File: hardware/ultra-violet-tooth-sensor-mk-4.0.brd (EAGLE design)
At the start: 51 x 23 mm, 13 parts, among them IC1 SI1145QFN10, U1 ADAFRUIT_BLUEFRUIT_LE_MICRO, U2 ADAFRUIT-SI1145-BREAKOUTHOLEY

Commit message: simblee based uvdosimeter
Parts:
- removed BATT: M02PTH-CENTERED-R+, A_butts:1X02-CENTER-R+
- removed IC1: SI1145QFN10, A_butts:SI1145
- removed POWER: SWITCH-SPDTPTH-RA-2.54MM, A_butts:SPDT-RA-2.54MM
- added BAT: M02JST-PTH-RA-R+, a_parts:JST-2-PH-RA-PTH-R+
- added C3, C8: 10u, a_parts:C0603
- added C4: 10nF, a_parts:C0603
- added C5: 4u7, a_parts:C0603
- added C6: 100n, a_parts:C0603
- added C7: 0.1uF, a_parts:C0603
- added CHRG, DONE: LED0603, a_parts:LED-0603
- added D1: (no value), a_parts:SOD123-SCHOTTKY
- added DISP1: ER-OLED0.49-1FOLDED-SAME, a_parts:ER-OLED0.49-1-FOLDED-SAME
- added Q1: (no value), a_parts:SOT23
- added R1: 10K, a_parts:R0603
- added R4: 1K, a_parts:R0603
- added R5: 100K, a_parts:R0603
- added RESET: SPST-NO-TACTSMD-TINIER, a_parts:TACTILE_SWITCH_SMD_TINY
- added U3: MCP73831T-2ACI/OT, a_parts:SOT95P280X145-5N
- added U4: V_REG_SOT-23-5AS13985, a_parts:SOT23-5
- added U5: VEML6075, a_parts:OPLGA4
- added U6: TCS3400DFN6, a_parts:TCS3400_DFN6
- added USB: (no value), a_parts:FCI-10103594-USB-MICRO-B-LESS
- C1: device A_butts:C0805 -> a_parts:C0603
- C2: value 0.1uF -> 10u; device A_butts:C0805 -> a_parts:C0603
- FRAME1: value (none) -> FRAME-LETTERNO_PACKAGE
- R2: value 100k -> 330R; device A_butts:R0805 -> a_parts:R0603
- R3: value 100k -> 2K; device A_butts:R0805 -> a_parts:R0603
- U1: value ADAFRUIT_BLUEFRUIT_LE_MICRO -> SIMBLEE-RFD77101; device A_butts:ADAFRUIT_BLUEFRUIT_LE_MICRO -> a_parts:RFD77101
- U2: value ADAFRUIT-SI1145-BREAKOUTHOLEY -> FTS31XS-U; device A_butts:ADAFRUIT-SI1145-BREAKOUT -> a_parts:SSOP20_L
- moved R2 135.7 mm to (-38.4, -67.8), turned to 0 degrees
- moved R3 125.3 mm to (-38.4, -58.9), turned to 0 degrees
- moved U2 46.9 mm to (-4.50, -14.7), turned to 0 degrees
- moved U1 31.5 mm to (-5.30, 4.80)
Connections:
- removed net SCL: IC1.SCL, R3.1, U1.3/SCL, U2.SCL
- removed net SDA: IC1.SDA, R2.1, U1.2/SDA, U2.SDA
- new net DTR: C4.1
- new net N$2: CHRG.C, DONE.A, R2.1
- new net N$3: U2.11, USB.3
- new net N$4: U2.12, USB.2
- new net N$5: R3.2, U3.5
- new net N$6: R2.2, U3.1
- new net N$9: C6.1, U4.3
- new net RESET: C4.2, R1.1, RESET.P$2, U1.8
- new net VBAT: BAT.2, C5.1, Q1.3, U3.3
- new net VIN: C2.1, D1.C, Q1.2, U4.1, U4.4
- new net VUSB: CHRG.A, D1.A, Q1.1, R5.2, U2.15, U3.4, USB.1
- net 3.3V: now also C3.1, C7.1, R1.2, U1.7, U2.14, U2.3, U4.5; no longer C2.1, IC1.VCC@1, IC1.VCC@2, IC1.VCC@3, R2.2, R3.2, U1.3V3, U2.3V3_OUT
- net GND: now also BAT.1, C3.2, C5.2, C6.2, C7.2, DONE.C, R3.1, R5.1, RESET.P$1, U1.1, U1.19, U1.2, U1.30, U1.4, U1.42, U1.43, U1.44, U1.45, U1.6, U2.16, U2.6, U3.2, U4.2, USB.5; no longer IC1.GND, U1.GND@1, U1.GND@2, U1.GND@3, U2.GND

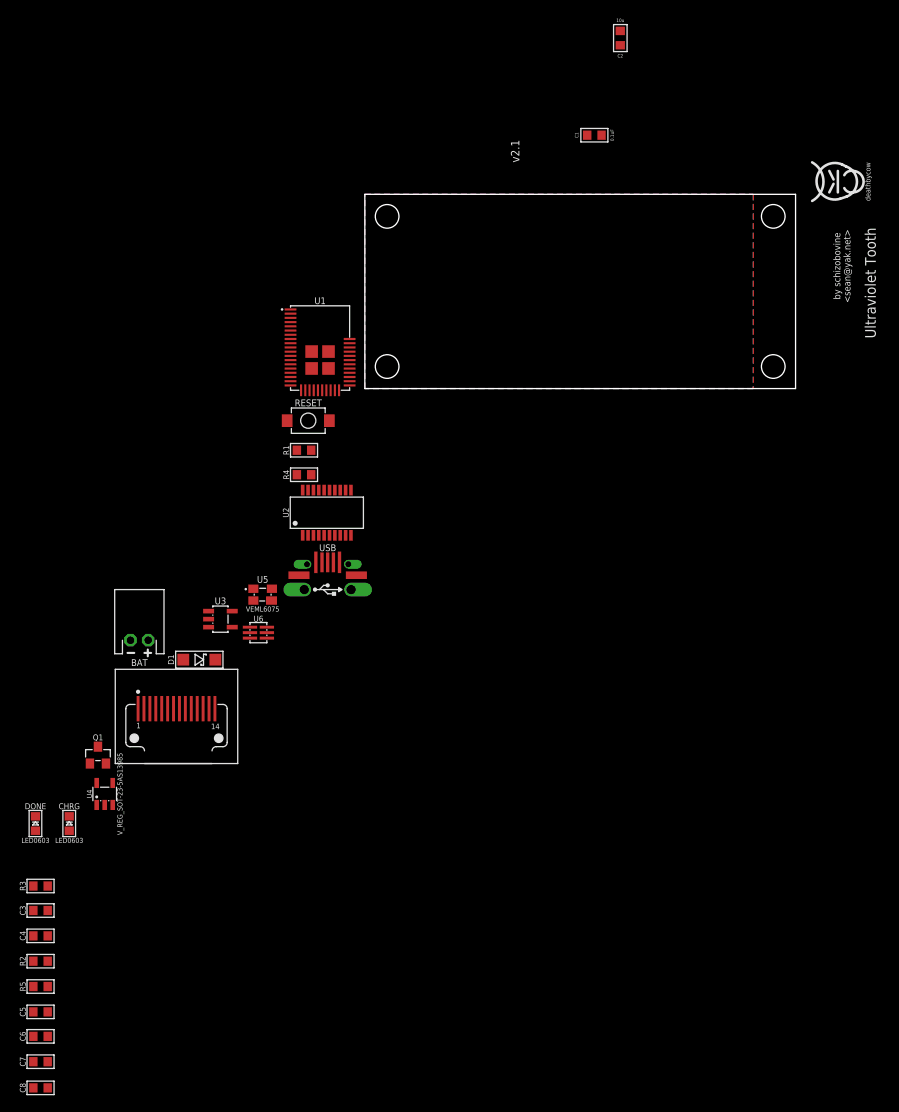
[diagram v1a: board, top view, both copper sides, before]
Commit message: more fiddling, need smaller usb to uart chip
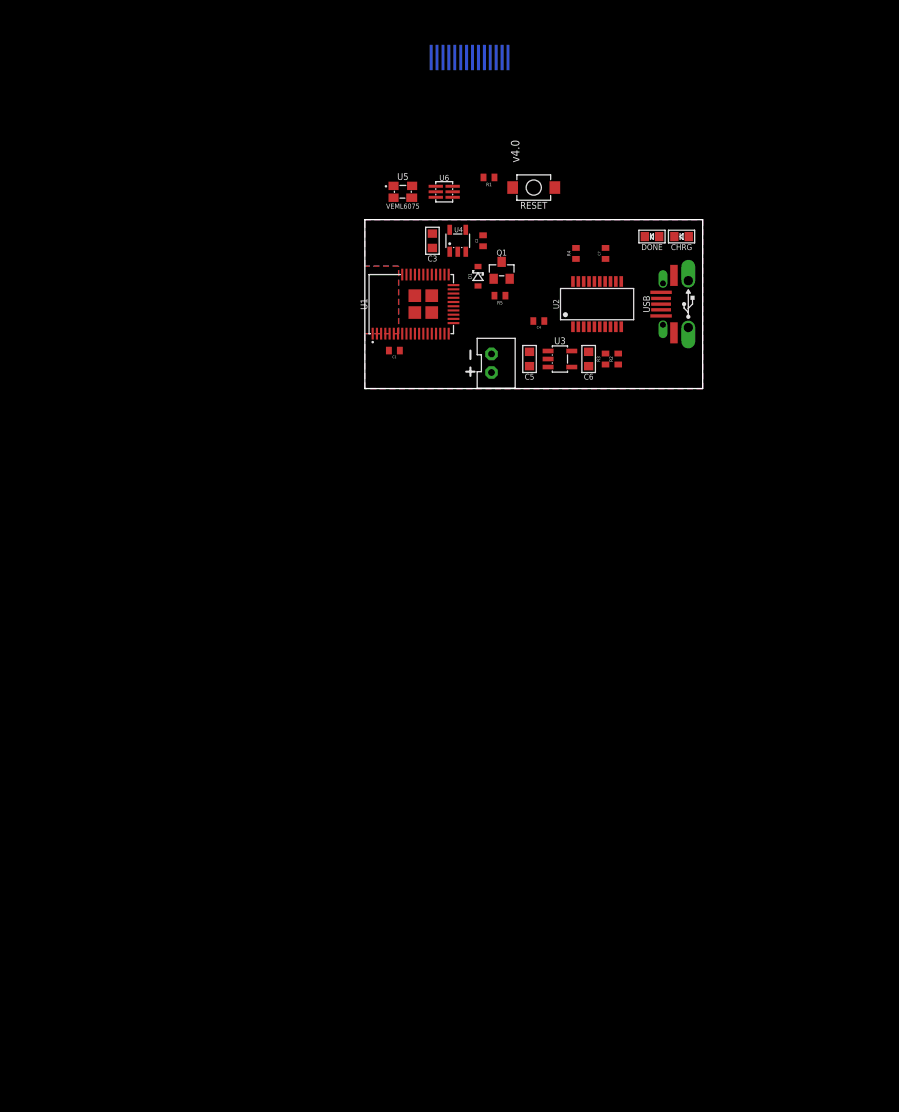
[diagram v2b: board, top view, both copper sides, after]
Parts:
- removed C8: 10u, a_parts:C0603
- removed U$1: (no value), A_butts:CC-BY-SA-4.0-NO-URL
- removed U$5: (no value), A_butts:COW_SMALL
- removed U$6: (no value), A_butts:OSHWLOGO_SILKONLY
- BAT: value M02JST-PTH-RA-R+ -> M02JST-PH-VERT-R+; device a_parts:JST-2-PH-RA-PTH-R+ -> a_parts:JST-2-PH-VERT-PTH-R+
- C1, C4, C7: device a_parts:C0603 -> a_parts:C0402
- C2: value 10u -> 1u; device a_parts:C0603 -> a_parts:C0402
- C6: value 100n -> 4u7
- D1: value (none) -> BAT54J; device a_parts:SOD123-SCHOTTKY -> a_parts:SOD323-SCHOTTKY
- R1, R2, R3, R4, R5: device a_parts:R0603 -> a_parts:R0402
- moved C7 116.8 mm to (28.5, 16.0), turned to 90 degrees
- moved C6 103.2 mm to (26.5, 3.50), turned to 90 degrees
- moved DONE 100.8 mm to (34.0, 18.0), turned to 90 degrees
- moved CHRG 100.4 mm to (37.5, 18.0), turned to 90 degrees
- moved R2 98.8 mm to (30.0, 3.50), turned to 90 degrees
- moved R5 98.2 mm to (16.0, 11.0), turned to 180 degrees
- moved C5 96.6 mm to (19.5, 3.50), turned to 90 degrees
- moved C4 93.7 mm to (20.6, 8.00), turned to 180 degrees
- moved C3 91.9 mm to (8.00, 17.5), turned to 90 degrees
- moved R3 91.5 mm to (28.5, 3.50), turned to 90 degrees
- moved DISP1 84.5 mm to (12.4, 39.2), flipped to the bottom
- moved U4 77.7 mm to (11.0, 17.5)
- moved Q1 74.7 mm to (16.2, 14.0)
- moved U6 56.6 mm to (9.40, 23.3)
- moved D1 56.1 mm to (13.4, 13.3), turned to 90 degrees
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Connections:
- net N$3 renamed D+
- net N$4 renamed D-
- net RESET renamed !RESET
- removed net N$9: C6.1, U4.3
- new net N$3: R4.2, U1.25
- new net N$4: C7.1, U2.13, U2.14, U2.3
- new net RXI: R4.1, U2.20
- new net TXO: U1.23, U2.4
- net 3.3V: no longer C7.1, U2.14, U2.3
- net DTR: now also U2.1
- net VUSB: now also C6.1
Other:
- board size 51 x 23 mm -> 40 x 20 mm
- board text removed: "Ultraviolet Tooth"
- board text removed: "by schizobovine <sean@yak.net>"

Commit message: new board work
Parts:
- removed DONE: LED0603, a_parts:LED-0603
- BAT: value M02JST-PH-VERT-R+ -> M02JST-2MM-SMT; device a_parts:JST-2-PH-VERT-PTH-R+ -> a_parts:JST-2-SMD
- C2: device a_parts:C0402 -> a_parts:C0603-TIGHTER
- C3, C5, C6: device a_parts:C0603 -> a_parts:C0603-TIGHTER
- CHRG: value LED0603 -> LED0603-TIGHT; device a_parts:LED-0603 -> a_parts:LED-0603-TIGHT
- U4: value V_REG_SOT-23-5AS13985 -> V_REG_SOT-23-5SPX3819
- USB: value (none) -> USB-AB-SHIELDFCI-10118193-USB-MICRO-B; device a_parts:FCI-10103594-USB-MICRO-B-LESS -> a_parts:FCI-10118193-USB-MICRO-B
- moved BAT 35.2 mm to (48.5, 13.7), turned to 180 degrees
- moved USB 0.40 mm to (38.7, 10.0)
- moved CHRG 0.10 mm to (37.5, 17.9), turned to 270 degrees
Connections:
- net GND: now also BAT.2; no longer BAT.1, DONE.C
- net N$2: no longer DONE.A
- net VBAT: now also BAT.1; no longer BAT.2
- net VIN: now also U4.3; no longer U4.4
